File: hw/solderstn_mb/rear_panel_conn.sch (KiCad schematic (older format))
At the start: 0 parts

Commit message: Summer vacation 2020 updates: * Front panel design rev 1 complete (incl Experimental outer board with optional linear touch sensors) * MB schematics AlmostDone(tm) - 'old' pinout supporting only one Rotary encoder * Lots of docs for new stuff
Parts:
- added D1201, D1202, D1203: SLESD5Z5V, symbol customlib_mj:SLESD5Z5V
- added J1201: USB_A-TE_1-292303-1, customlib_mj_fp:TE_1-292303-1, symbol customlib_mj:USB_A-TE_1-292303-1
- added J1202: DB9_Male_MountingHoles, Connector_Dsub:DSUB-9_Male_Horizontal_P2.77x2.84mm_EdgePinOffset9.90mm_Housed_MountingHolesOffset11.32mm, symbol Connector:DB9_Male_MountingHoles
- added J1203: USB_B-TE_1734346-1, customlib_mj_fp:TE_1734346, symbol customlib_mj:USB_B-TE_1734346-1
- added U1201, U1202: USBLC6-2SC6, TO_SOT_Packages_SMD:SOT-23-6, symbol customlib_mj:USBLC6-2SC6
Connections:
- net labels added: CH_A_HEATER_1, CH_A_HEATER_2, CH_A_TC1, CH_A_TC2_KTY, CH_B_HEATER_1, CH_B_HEATER_2, CH_B_TC1, CH_B_TC2_KTY, DBGUART_RX, DBGUART_TX, GND, MCU_BOOT0, SWCLK, SWDIO, USB1_DM, USB1_DP, USB2_DM, USB2_DP, VBUS, VBUS_2, VDD, ~EXT_RSTn~
- wire segments 0 -> 34
- no-connect marks 0 -> 1
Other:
- note added: "DBGUART / SWD (dsub-9?)\nFM-ant? (AM-ferrit extern..?)\nUSB1 (device)\nUSB2 (host)\nForce Bootloader/rst\n2x Amphenol Weller-jacks!"
- note added: "Notes:\nAudio-jack 3.5mm - located on audio page\nRJ45 ethernet - located on ethernet page\n"
- note added: "TODO:\n* Add 74HC*-buffer for \nthe external signals\n* Also ESD TVSs"
- note added: "TODO:\n* ESD for USBs"

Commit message: * Remove separate REED_PULLUP_EN pin; instead bias the Reedswitches with the per-channel KTY bias (buffered Vref) * Add separate mini cut-out sub-PCB for 3.5 headphone connector at back-panel (must be angled vertical to fit in panel) * Some ESD and buffering on back panel
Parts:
- removed D1201, D1202, D1203: SLESD5Z5V, symbol customlib_mj:SLESD5Z5V
- added C?: 100n, symbol Device:C_Small
- added D?: SP0505BAHT, Package_TO_SOT_SMD:SOT-23-6, symbol Power_Protection:SP0505BAHT
- added J?: Conn_02x03_Odd_Even, Connector_PinSocket_2.54mm:PinSocket_2x03_P2.54mm_Vertical, symbol Connector_Generic:Conn_02x03_Odd_Even
- added R? (x4): 1k, symbol Device:R_Small
- added R? (x2): 100, symbol Device:R_Small
- added U? (x3): 74LVC2G17, symbol customlib_mj:74LVC2G17
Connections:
- net labels added: Audio_L, Audio_L_int, Audio_R, Audio_R_int
- wire segments 34 -> 94
- no-connect marks 1 -> 0
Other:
- note added: "(Dummies!)"
- note added: "Headphone 3.5mm connector on\na break-away sub-PCB.\nAudio signals get routed out to\nthe 3.5mm connector, through\nthe plug-switches and optionally\nback to internal speakers conns\nif there's no plug inserted"
- note removed: "TODO:\n* Add 74HC*-buffer for \nthe external signals\n* Also ESD TVSs"
- note removed: "TODO:\n* ESD for USBs"
- moved on the sheet: J1201, J1202, J1203, U1201, U1202

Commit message: * pinheader/socket for headphone sub-PCB 2x3 -> 2x5 (greater mechanical stability) * printed WIP-schematics pdf for 08-19
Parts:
- removed J?: Conn_02x03_Odd_Even, Connector_PinSocket_2.54mm:PinSocket_2x03_P2.54mm_Vertical, symbol Connector_Generic:Conn_02x03_Odd_Even
- added J?: Conn_02x05_Odd_Even, Connector_PinSocket_2.54mm:PinSocket_2x05_P2.54mm_Vertical, symbol Connector_Generic:Conn_02x05_Odd_Even
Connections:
- wire segments 94 -> 96
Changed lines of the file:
@@
 F5 "Audio_int_R" O R 9400 1500 50
 $EndSheet
-$Comp
-L Connector_Generic:Conn_02x03_Odd_Even J?
-U 1 1 5F920BA3
-P 7250 1350
-F 0 "J?" H 7300 1667 50  0000 C CNN
-F 1 "Conn_02x03_Odd_Even" H 7300 1576 50  0000 C CNN
-F 2 "Connector_PinSocket_2.54mm:PinSocket_2x03_P2.54mm_Vertical" H 7250 1350 50  0001 C CNN
-F 3 "~" H 7250 1350 50  0001 C CNN
-	1    7250 1350
-	1    0    0    -1
-$EndComp
 Text HLabel 6800 1250 0    50   Input ~ 0
 Audio_L
@@
 Text Notes 10100 1500 1    50   ~ 0
 (Dummies!)
-Text Notes 7450 2150 0    50   ~ 10
+Text Notes 7500 2350 0    50   ~ 10
 Headphone 3.5mm connector on\na break-away sub-PCB.\nAudio signals get routed out to\nthe 3.5mm connector, through\nthe plug-switches and optionally\nback to internal speakers conns\nif there's no plug inserted
 Wire Wire Line
@@
 Wire Wire Line
 	3750 5000 4050 5000
+$Comp
+L Connector_Generic:Conn_02x05_Odd_Even J?
+U 1 1 5FA2CF9B
+P 7250 1450
+F 0 "J?" H 7300 1867 50  0000 C CNN
+F 1 "Conn_02x05_Odd_Even" H 7300 1776 50  0000 C CNN
+F 2 "Connector_PinSocket_2.54mm:PinSocket_2x05_P2.54mm_Vertical" H 7250 1450 50  0001 C CNN
+F 3 "~" H 7250 1450 50  0001 C CNN
+	1    7250 1450
+	1    0    0    -1
+$EndComp
+$Comp
+L power:GND #PWR?
+U 1 1 5FA2DA97
+P 7000 1550
+F 0 "#PWR?" H 7000 1300 50  0001 C CNN
+F 1 "GND" H 7000 1400 50  0000 C CNN
+F 2 "" H 7000 1550 50  0001 C CNN
+F 3 "" H 7000 1550 50  0001 C CNN
+	1    7000 1550
+	0    1    1    0
+$EndComp
+$Comp
+L power:GND #PWR?
+U 1 1 5FA2DDB5
+P 7600 1550
+F 0 "#PWR?" H 7600 1300 50  0001 C CNN
+F 1 "GND" H 7600 1400 50  0000 C CNN
+F 2 "" H 7600 1550 50  0001 C CNN
+F 3 "" H 7600 1550 50  0001 C CNN
+	1    7600 1550
+	0    -1   -1   0
+$EndComp
+Wire Wire Line
+	7600 1550 7550 1550
+Wire Wire Line
+	7050 1550 7000 1550
 $EndSCHEMATC

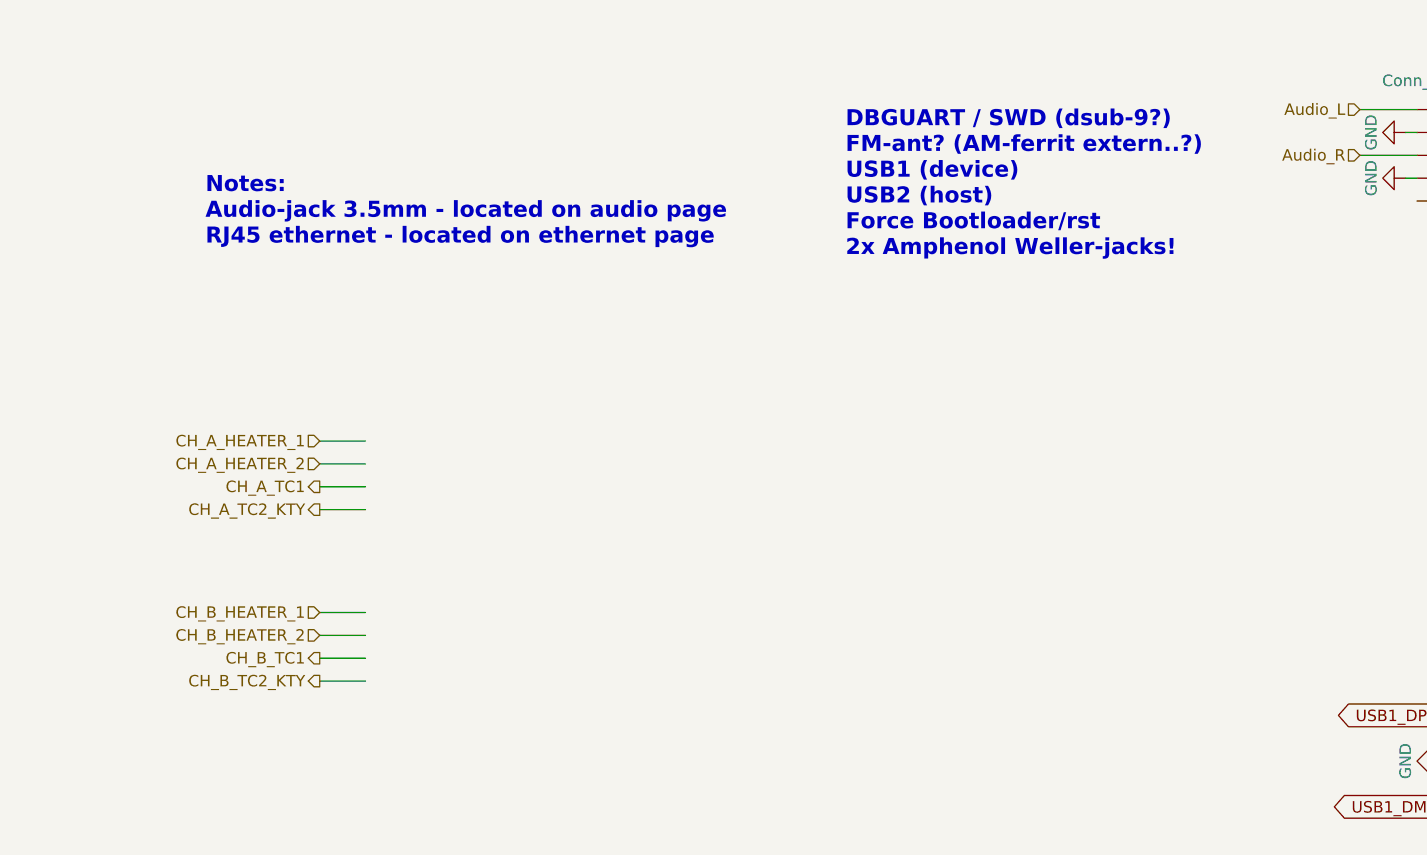
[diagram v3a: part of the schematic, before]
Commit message: * Added Molex connectors (PwrLED-conn, DC-in, FM-ant.) * Renamed Si4735 doc dir
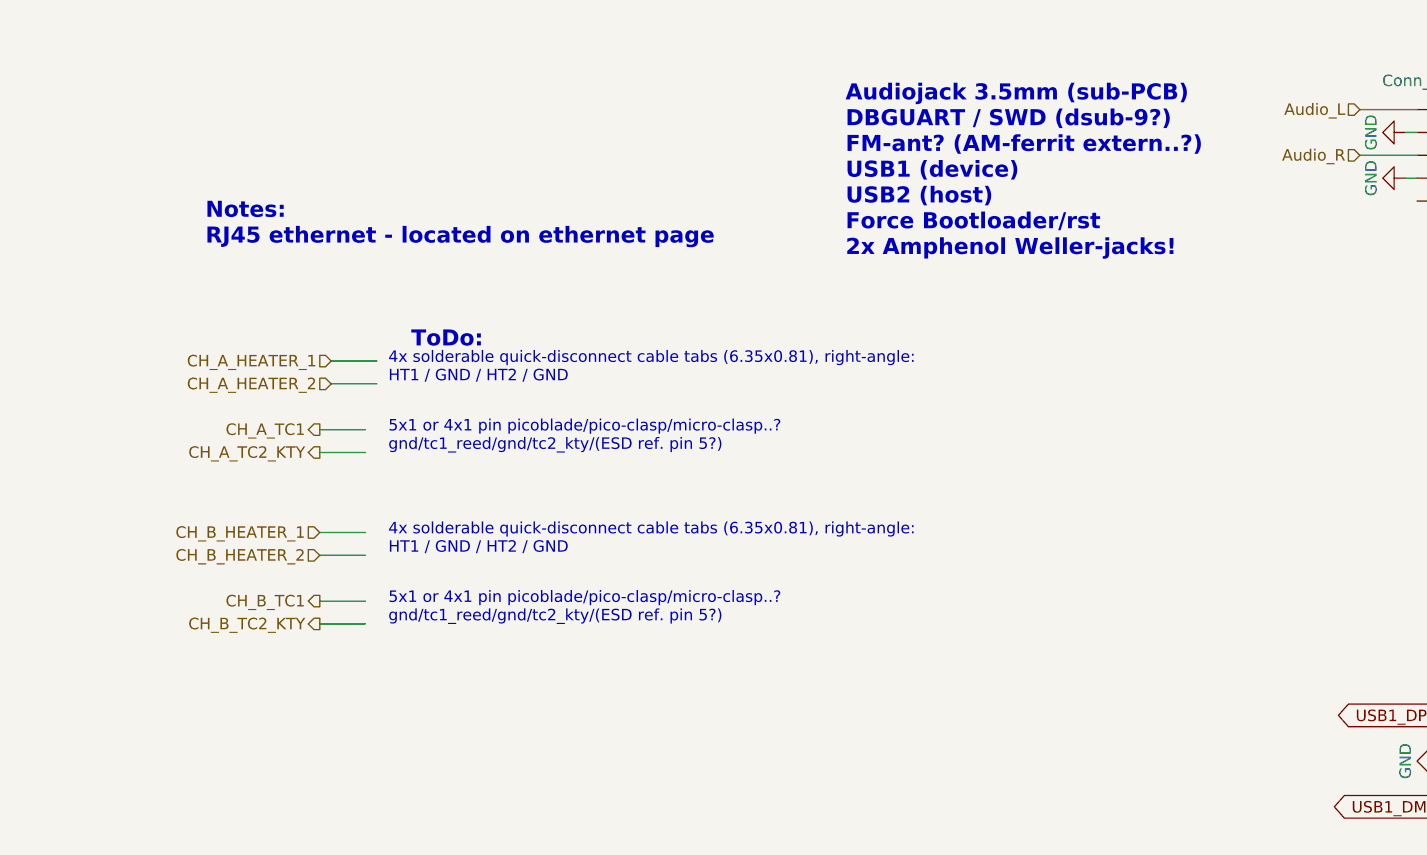
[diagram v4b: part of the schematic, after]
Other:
- note added: "4x solderable quick-disconnect cable tabs (6.35x0.81), right-angle:\nHT1 / GND / HT2 / GND\n"
- note added: "5x1 or 4x1 pin picoblade/pico-clasp/micro-clasp..?\ngnd/tc1_reed/gnd/tc2_kty/(ESD ref. pin 5?)"
- note added: "Audiojack 3.5mm (sub-PCB)\nDBGUART / SWD (dsub-9?)\nFM-ant? (AM-ferrit extern..?)\nUSB1 (device)\nUSB2 (host)\nForce Bootloader/rst\n2x Amphenol Weller-jacks!"
- note added: "Notes:\nRJ45 ethernet - located on ethernet page\n"
- note added: "ToDo:"
- note removed: "DBGUART / SWD (dsub-9?)\nFM-ant? (AM-ferrit extern..?)\nUSB1 (device)\nUSB2 (host)\nForce Bootloader/rst\n2x Amphenol Weller-jacks!"
- note removed: "Notes:\nAudio-jack 3.5mm - located on audio page\nRJ45 ethernet - located on ethernet page\n"
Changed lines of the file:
@@
 Comment4 ""
 $EndDescr
-Text HLabel 2250 2700 0    50   Input ~ 0
+Text HLabel 2300 2350 0    50   Input ~ 0
 CH_A_HEATER_1
-Text HLabel 2250 2800 0    50   Input ~ 0
+Text HLabel 2300 2450 0    50   Input ~ 0
 CH_A_HEATER_2
-Text HLabel 2250 2900 0    50   Output ~ 0
+Text HLabel 2250 2650 0    50   Output ~ 0
 CH_A_TC1
-Text HLabel 2250 3000 0    50   Output ~ 0
+Text HLabel 2250 2750 0    50   Output ~ 0
 CH_A_TC2_KTY
-Text HLabel 2250 3450 0    50   Input ~ 0
+Text HLabel 2250 3100 0    50   Input ~ 0
 CH_B_HEATER_1
-Text HLabel 2250 3550 0    50   Input ~ 0
+Text HLabel 2250 3200 0    50   Input ~ 0
 CH_B_HEATER_2
-Text HLabel 2250 3650 0    50   Output ~ 0
+Text HLabel 2250 3400 0    50   Output ~ 0
 CH_B_TC1
-Text HLabel 2250 3750 0    50   Output ~ 0
+Text HLabel 2250 3500 0    50   Output ~ 0
 CH_B_TC2_KTY
 Wire Wire Line
-	2250 2700 2450 2700
-Wire Wire Line
-	2250 2800 2450 2800
-Wire Wire Line
-	2250 2900 2450 2900
-Wire Wire Line
-	2250 3000 2450 3000
-Wire Wire Line
-	2250 3450 2450 3450
-Wire Wire Line
-	2250 3550 2450 3550
-Wire Wire Line
-	2250 3650 2450 3650
-Wire Wire Line
-	2250 3750 2450 3750
+	2300 2350 2500 2350
+Wire Wire Line
+	2300 2450 2500 2450
+Wire Wire Line
+	2250 2650 2450 2650
+Wire Wire Line
+	2250 2750 2450 2750
+Wire Wire Line
+	2250 3100 2450 3100
+Wire Wire Line
+	2250 3200 2450 3200
+Wire Wire Line
+	2250 3400 2450 3400
+Wire Wire Line
+	2250 3500 2450 3500
 Text Notes 4550 1900 0    70   ~ 14
-DBGUART / SWD (dsub-9?)\nFM-ant? (AM-ferrit extern..?)\nUSB1 (device)\nUSB2 (host)\nForce Bootloader/rst\n2x Amphenol Weller-jacks!
+Audiojack 3.5mm (sub-PCB)\nDBGUART / SWD (dsub-9?)\nFM-ant? (AM-ferrit extern..?)\nUSB1 (device)\nUSB2 (host)\nForce Bootloader/rst\n2x Amphenol Weller-jacks!
 Text GLabel 3150 5600 0    50   Output ~ 0
 ~EXT_RSTn~
@@
 MCU_BOOT0
 Text Notes 1750 1850 0    70   ~ 14
-Notes:\nAudio-jack 3.5mm - located on audio page\nRJ45 ethernet - located on ethernet page\n
+Notes:\nRJ45 ethernet - located on ethernet page\n
 $Comp
 L customlib_mj:USB_A-TE_1-292303-1 J1201
@@
 Wire Wire Line
 	7050 1550 7000 1550
+Text Notes 2550 2750 0    50   ~ 0
+5x1 or 4x1 pin picoblade/pico-clasp/micro-clasp..?\ngnd/tc1_reed/gnd/tc2_kty/(ESD ref. pin 5?)
+Text Notes 2550 2450 0    50   ~ 0
+4x solderable quick-disconnect cable tabs (6.35x0.81), right-angle:\nHT1 / GND / HT2 / GND\n
+Text Notes 2550 3500 0    50   ~ 0
+5x1 or 4x1 pin picoblade/pico-clasp/micro-clasp..?\ngnd/tc1_reed/gnd/tc2_kty/(ESD ref. pin 5?)
+Text Notes 2550 3200 0    50   ~ 0
+4x solderable quick-disconnect cable tabs (6.35x0.81), right-angle:\nHT1 / GND / HT2 / GND\n
+Text Notes 2650 2300 0    70   ~ 14
+ToDo:
 $EndSCHEMATC
